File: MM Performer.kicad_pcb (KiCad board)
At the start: 4 copper layers, 74.8 x 84.8 mm, 41 parts, among them IC1 68000D, J1 VCC, J2 GND, U1 MC68030RC, U2 MC68881FN-SOC, U3 ATF16V8BJ, U4 ATF16V8BJ, U5 ATF16V8BJ, U6 ATF16V8BJ, U7 ATF16V8BJ

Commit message: Draw PCB
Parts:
- U3, U4, U5, U6: footprint footprints:PLCC-20_THT-Socket -> Package_LCC:PLCC-20_SMD-Socket; moved to B.Cu
- moved R4 17.4 mm to (50.2, 99.2)
- moved R9 13.8 mm to (47.4, 120.9)
- moved R16 13.8 mm to (52.7, 120.9)
- moved C9 11.7 mm to (50.0, 127.5)
- moved C8 10.0 mm to (50.2, 106.0)
- moved C7 8.38 mm to (50.2, 84.6)
- moved U3 7.37 mm to (50.0, 127.5)
- moved C5 6.60 mm to (50.2, 63.1)
- moved U4 5.67 mm to (50.2, 106.0)
- moved U6 3.98 mm to (50.2, 84.6)
- moved U5 2.29 mm to (50.2, 63.1)
- moved U1 0.18 mm to (81.7, 118.9)
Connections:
- U1 pad C5: (no net) -> GND
- U1 pad C6: (no net) -> VCC
- U1 pad C7: (no net) -> GND
- U1 pad C9: (no net) -> GND
- U1 pad D4: (no net) -> VCC
- U1 pad E3: (no net) -> GND
- U1 pad F2: (no net) -> VCC
- U1 pad F3: (no net) -> GND
- U1 pad G3: (no net) -> GND
- U1 pad H3: (no net) -> VCC
- U1 pad J3: (no net) -> GND
- U1 pad K4: (no net) -> VCC
- U1 pad L5: (no net) -> GND
- U1 pad L6: (no net) -> VCC
- U1 pad L7: (no net) -> GND
- U1 pad L8: (no net) -> GND
- U1 pad L9: (no net) -> GND
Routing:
- net GND: track 542.5 -> 659.5 mm, vias 10 -> 18
- net VCC: track 749.4 -> 654.6 mm, vias 9 -> 10
- net /A21: track 83.0 -> 128.4 mm, vias 2 -> 3
- net /A0: track 73.1 -> 105.2 mm, vias 2 -> 4
- net /D17: track 130.2 -> 99.5 mm, vias 2 -> 3
- net //R/W: track 127.4 -> 157.1 mm, vias 0 -> 5
- net /D20: track 127.8 -> 100.0 mm, vias 5 -> 2
- net /D7: track 44.1 -> 69.6 mm, vias 1 -> 3
- net /D14: track 68.6 -> 44.3 mm, vias 5 -> 0
- net /C8M.PDS: track 82.2 -> 105.5 mm, vias 0 -> 3
- net /N$1: track 13.2 -> 35.3 mm, vias 0 -> 3
- net /D16: track 119.8 -> 98.1 mm, vias 1 -> 4
- net //RESET_00: track 35.3 -> 53.8 mm, vias 0 -> 2
- net /A23: track 83.2 -> 101.5 mm, vias 1 -> 3
- net /D9: track 42.1 -> 59.9 mm, vias 1 -> 2
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- added copper zone on B.Cu, net GND
- added copper zone on F.Cu, net GND
- added copper zone on In1.Cu, net GND
- added copper zone on In2.Cu, net GND

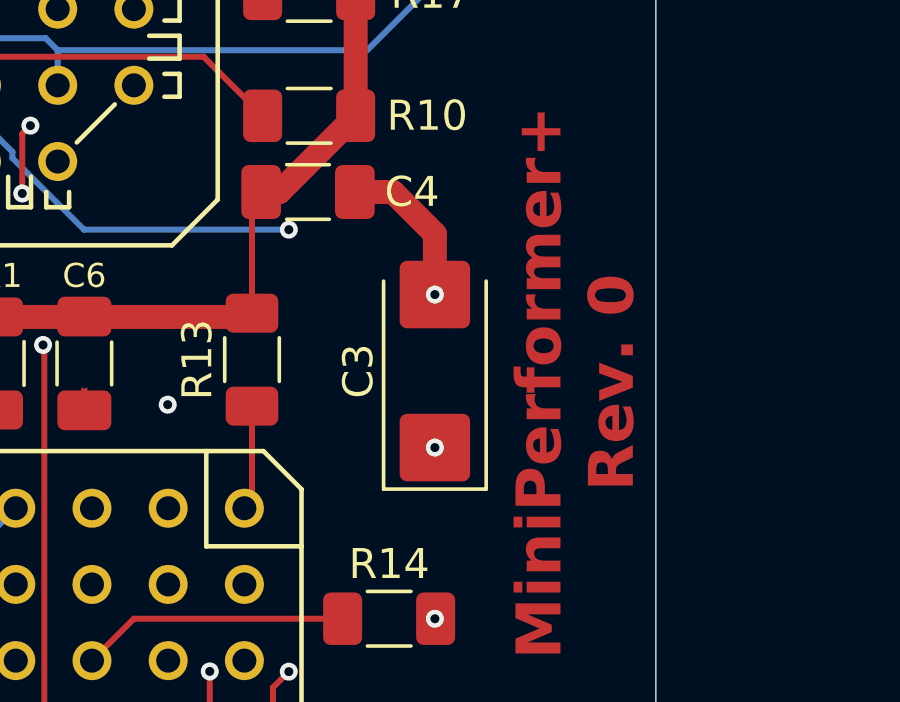
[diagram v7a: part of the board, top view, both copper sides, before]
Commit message: Change width of a VCC trace
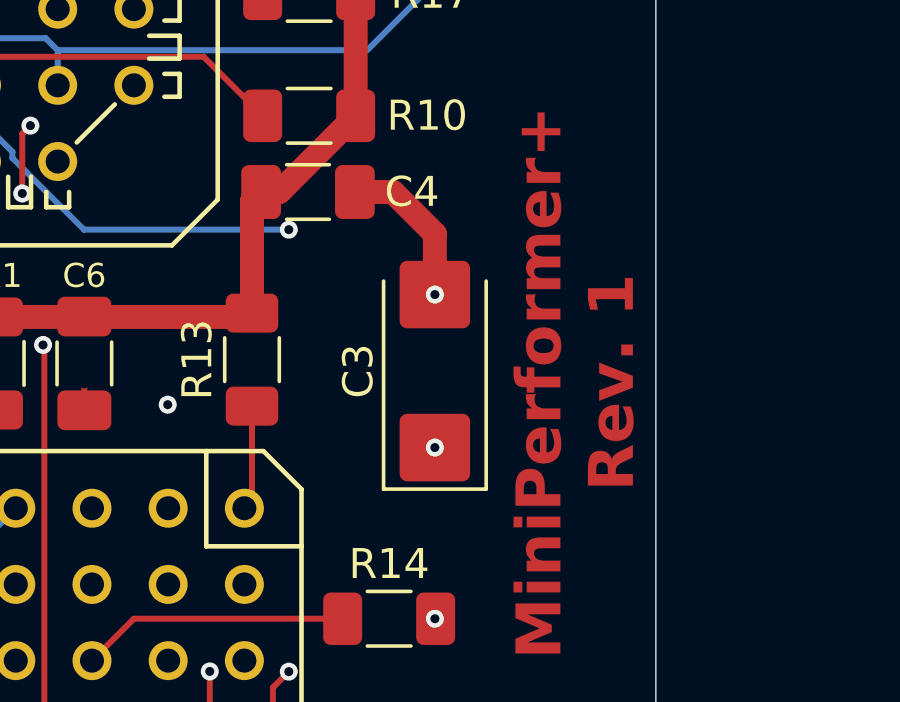
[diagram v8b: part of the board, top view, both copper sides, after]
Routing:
- net VCC: track 654.6 -> 655.3 mm
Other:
- board text added: "MiniPerformer+ Rev. 1"
- board text removed: "MiniPerformer+ Rev. 0"
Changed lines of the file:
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@@
 		(layer "Edge.Cuts")
 	)
-	(gr_text "MiniPerformer+\nRev. 0"
+	(gr_text "MiniPerformer+\nRev. 1"
 		(at 107.95 99.441 90)
 		(layer "F.Cu")
@@
 		)
 	)
-	(gr_text "MiniPerformer+\nRev. 0"
+	(gr_text "MiniPerformer+\nRev. 1"
 		(at 107.95 99.441 90)
 		(layer "F.Mask")
@@
 	)
 	(segment
-		(start 97.155 97.129)
-		(end 97.155 93.7005)
-		(width 0.2)
-		(layer "F.Cu")
-		(net 1)
-	)
-	(segment
 		(start 98.07 93.091)
 		(end 100.61 90.551)
@@
 		(end 103.2855 133.985)
 		(width 0.2)
+		(layer "F.Cu")
+		(net 1)
+	)
+	(segment
+		(start 97.155 93.395)
+		(end 97.459 93.091)
+		(width 0.8)
 		(layer "F.Cu")
 		(net 1)
@@
 		(width 0.8)
 		(layer "F.Cu")
+		(net 1)
+	)
+	(segment
+		(start 97.155 97.129)
+		(end 97.155 93.395)
+		(width 0.8)
+		(layer "F.Cu")
